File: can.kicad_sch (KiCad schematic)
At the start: 4 parts, among them U8 SN65HVD230

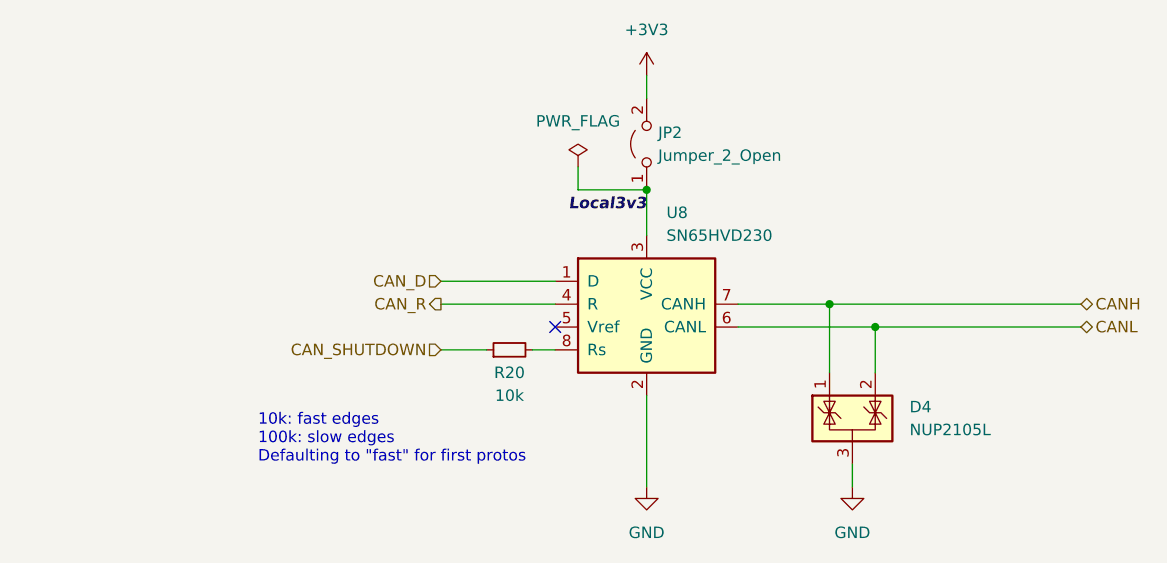
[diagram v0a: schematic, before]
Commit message: push forwards: clock muxing, filling in blanks
Finished off the ethernet section finally.
Sorted a solution to the 25M phy clocks required for ethercat
Connected CAN as per existing hardware (and fixed a bug in speed mode)
Sorted out bypassing for MCU
Added more thoughts on the external interfaces
Started on a 24V supply
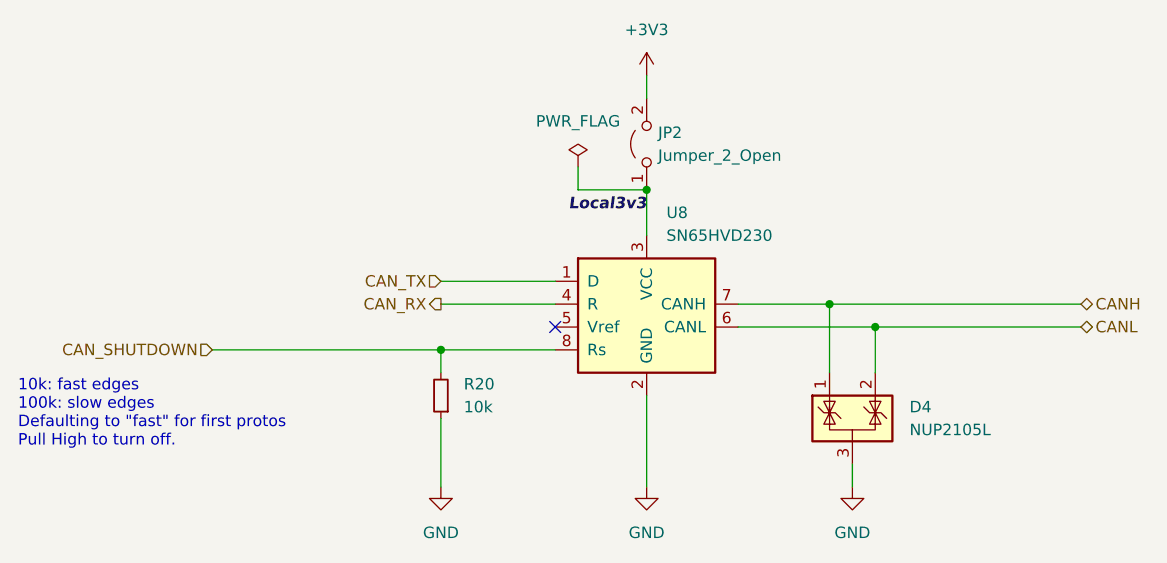
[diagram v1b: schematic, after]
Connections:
- net CAN_SHUTDOWN: now also R20.2, U8.8 (Rs); no longer R20.1
- net GND: now also R20.1
- net CAN_D renamed CAN_TX
- net CAN_R renamed CAN_RX
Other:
- note added: "10k: fast edges 100k: slow edges Defaulting to "fast" for first protos Pull High to turn off."
- note removed: "10k: fast edges 100k: slow edges Defaulting to "fast" for first protos"
- moved on the sheet: R20
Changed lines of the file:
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@@
 	(generator_version "10.0")
 	(paper "A4")
-	(text "10k: fast edges\n100k: slow edges\nDefaulting to \"fast\" for first protos"
+	(text "10k: fast edges\n100k: slow edges\nDefaulting to \"fast\" for first protos\nPull High to turn off."
 		(exclude_from_sim no)
-		(at 81.28 106.68 0)
+		(at 54.61 104.902 0)
 		(effects
 			(font
@@
 			(justify left bottom)
 		)
+	)
+	(junction
+		(at 101.6 93.98)
+		(diameter 0)
+		(color 0 0 0 0)
 	)
 	(junction
@@
 	(wire
 		(pts
-			(xy 101.6 93.98) (xy 106.68 93.98)
-		)
-		(stroke
-			(width 0)
-			(type default)
-		)
-	)
-	(wire
-		(pts
-			(xy 111.76 93.98) (xy 114.3 93.98)
+			(xy 76.2 93.98) (xy 101.6 93.98)
 		)
 		(stroke
@@
 	(wire
 		(pts
+			(xy 101.6 93.98) (xy 114.3 93.98)
+		)
+		(stroke
+			(width 0)
+			(type default)
+		)
+	)
+	(wire
+		(pts
 			(xy 149.86 91.44) (xy 149.86 96.52)
 		)
@@
 	(wire
 		(pts
+			(xy 101.6 101.6) (xy 101.6 109.22)
+		)
+		(stroke
+			(width 0)
+			(type default)
+		)
+	)
+	(wire
+		(pts
 			(xy 144.78 88.9) (xy 172.72 88.9)
 		)
@@
 		(pts
 			(xy 116.84 76.2) (xy 124.46 76.2)
+		)
+		(stroke
+			(width 0)
+			(type default)
+		)
+	)
+	(wire
+		(pts
+			(xy 101.6 96.52) (xy 101.6 93.98)
 		)
 		(stroke
@@
 	(hierarchical_label "CAN_SHUTDOWN"
 		(shape input)
-		(at 101.6 93.98 180)
+		(at 76.2 93.98 180)
 		(effects
 			(font
@@
 		)
 	)
-	(hierarchical_label "CAN_D"
+	(hierarchical_label "CAN_TX"
 		(shape input)
 		(at 101.6 86.36 180)
@@
 		)
 	)
-	(hierarchical_label "CAN_R"
+	(hierarchical_label "CAN_RX"
 		(shape output)
 		(at 101.6 88.9 180)
@@
 	(symbol
 		(lib_id "Device:R_Small")
-		(at 109.22 93.98 90)
+		(at 101.6 99.06 180)
 		(unit 1)
 		(body_style 1)
@@
 		(fields_autoplaced yes)
 		(property "Reference" "R20"
-			(at 109.22 96.52 90)
-			(show_name no)
-			(do_not_autoplace no)
-			(effects
-				(font
-					(size 1.27 1.27)
-				)
+			(at 104.14 97.7899 0)
+			(show_name no)
+			(do_not_autoplace no)
+			(effects
+				(font
+					(size 1.27 1.27)
+				)
+				(justify right)
 			)
 		)
 		(property "Value" "10k"
-			(at 109.22 99.06 90)
-			(show_name no)
-			(do_not_autoplace no)
-			(effects
-				(font
-					(size 1.27 1.27)
-				)
+			(at 104.14 100.3299 0)
+			(show_name no)
+			(do_not_autoplace no)
+			(effects
+				(font
+					(size 1.27 1.27)
+				)
+				(justify right)
 			)
 		)
 		(property "Footprint" "Resistor_SMD:R_0603_1608Metric"
-			(at 109.22 93.98 0)
+			(at 101.6 99.06 0)
 			(hide yes)
 			(show_name no)
@@
 		)
 		(property "Datasheet" ""
-			(at 109.22 93.98 0)
+			(at 101.6 99.06 0)
 			(hide yes)
 			(show_name no)
@@
 		)
 		(property "Description" ""
-			(at 109.22 93.98 0)
+			(at 101.6 99.06 0)
 			(show_name no)
 			(do_not_autoplace no)
@@
 		)
 		(property "MPN" "0603WAF1002T5E"
-			(at 109.22 93.98 0)
+			(at 101.6 99.06 0)
 			(hide yes)
 			(show_name no)
@@
 		)
 		(property "jlc-basic" "1"
-			(at 109.22 93.98 0)
+			(at 101.6 99.06 0)
 			(hide yes)
 			(show_name no)
@@
 		)
 		(property "lcsc#" "C25804"
-			(at 109.22 93.98 0)
+			(at 101.6 99.06 0)
 			(hide yes)
 			(show_name no)
@@
 		)
 		(property "lcsc2#" ""
-			(at 109.22 93.98 0)
+			(at 101.6 99.06 0)
 			(hide yes)
 			(show_name no)
@@
 					(unit 1)
 				)
+			)
+		)
+	)
+	(symbol
+		(lib_id "power:GND")
+		(at 101.6 109.22 0)
+		(unit 1)
+		(body_style 1)
+		(exclude_from_sim no)
+		(in_bom yes)
+		(on_board yes)
+		(in_pos_files yes)
+		(dnp no)
+		(fields_autoplaced yes)
+		(property "Reference" "#PWR062"
+			(at 101.6 115.57 0)
+			(hide yes)
+			(show_name no)
+			(do_not_autoplace no)
+			(effects
+				(font
+					(size 1.27 1.27)
+				)
+			)
+		)
+		(property "Value" "GND"
+			(at 101.6 114.3 0)
+			(show_name no)
+			(do_not_autoplace no)
+			(effects
+				(font
+					(size 1.27 1.27)
+				)
+			)
+		)
+		(property "Footprint" ""
+			(at 101.6 109.22 0)
+			(hide yes)
+			(show_name no)
+			(do_not_autoplace no)
+			(effects
+				(font
+					(size 1.27 1.27)
+				)
+			)
+		)
+		(property "Datasheet" ""
+			(at 101.6 109.22 0)
+			(hide yes)
+			(show_name no)
+			(do_not_autoplace no)
+			(effects
+				(font
+					(size 1.27 1.27)
+				)
+			)
+		)
+		(property "Description" ""
+			(at 101.6 109.22 0)
+			(show_name no)
+			(do_not_autoplace no)
+			(effects
+				(font
+					(size 1.27 1.27)
+				)
+			)
+		)
+		(pin "1"
+		)
+		(instances
+			(project "xmc-ecat-enet-twin"
+				(path "/f5c7c34d-e330-4aa5-be7e-80f0a3a977af/ad8b4270-a50e-4348-8863-ac523723f700"
+					(reference "#PWR062")
+					(unit 1)
+				)

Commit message: finish a 24V supply
went with a more modern one, plenty of room.  Should be pretty good now.
Went over and filled in a bunch of missing parts and things, cleaned up
as much as I could 0603 vs 0402 for most, updated some thigns to current
atomic part library.

still to go, the "pi" interface and some sort of spi/io interface?
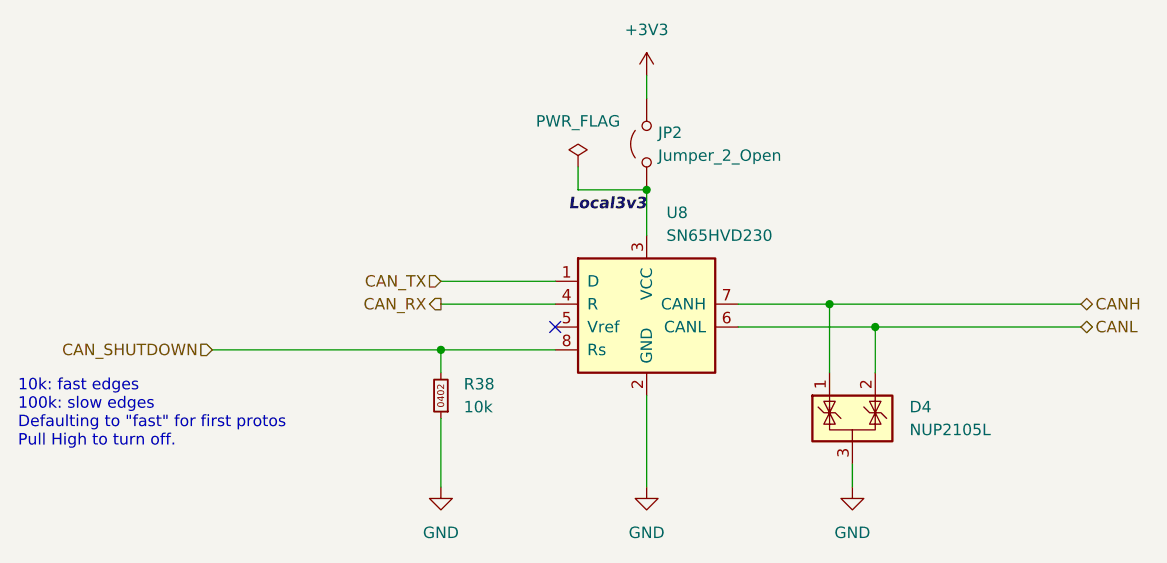
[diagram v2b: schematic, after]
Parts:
- removed R20: 10k, Resistor_SMD:R_0603_1608Metric, symbol Device:R_Small
- added R38: 10k, Resistor_SMD:R_0402_1005Metric, symbol karl-atomic-basic:KR0402_10k
- D4: LCSC Part # (none) -> C5261087; jlc-basic 0 -> (none); jlcbasic (none) -> 0; lcsc# C5261087 -> (none)
- U8: LCSC Part # (none) -> C12084; jlc-basic 1 -> (none); jlcbasic (none) -> basic; lcsc# C12084 -> (none)
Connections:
- net CAN_SHUTDOWN: now also R38.2
- net GND: now also R38.1
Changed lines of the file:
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@@
 	(wire
 		(pts
-			(xy 101.6 96.52) (xy 101.6 93.98)
+			(xy 149.86 91.44) (xy 172.72 91.44)
 		)
 		(stroke
@@
 	(wire
 		(pts
-			(xy 149.86 91.44) (xy 172.72 91.44)
+			(xy 101.6 93.98) (xy 101.6 96.52)
 		)
 		(stroke
@@
 	)
 	(symbol
-		(lib_id "Device:R_Small")
+		(lib_id "karl-atomic-basic:KR0402_10k")
 		(at 101.6 99.06 180)
 		(unit 1)
@@
 		(dnp no)
 		(fields_autoplaced yes)
-		(property "Reference" "R20"
+		(property "Reference" "R38"
 			(at 104.14 97.7899 0)
 			(show_name no)
@@
 			)
 		)
-		(property "Footprint" "Resistor_SMD:R_0603_1608Metric"
+		(property "Footprint" "Resistor_SMD:R_0402_1005Metric"
 			(at 101.6 99.06 0)
 			(hide yes)
@@
 			)
 		)
-		(property "Description" ""
+		(property "Description" "Resistor, 0402"
 			(at 101.6 99.06 0)
-			(show_name no)
-			(do_not_autoplace no)
-			(effects
-				(font
-					(size 1.27 1.27)
-				)
-			)
-		)
-		(property "MPN" "0603WAF1002T5E"
+			(hide yes)
+			(show_name no)
+			(do_not_autoplace no)
+			(effects
+				(font
+					(size 1.27 1.27)
+				)
+			)
+		)
+		(property "LCSC Part #" "C25744"
 			(at 101.6 99.06 0)
 			(hide yes)
@@
 			)
 		)
-		(property "jlc-basic" "1"
+		(property "MPN" "0402WGF1002TCE"
 			(at 101.6 99.06 0)
 			(hide yes)
@@
 			)
 		)
-		(property "lcsc#" "C25804"
+		(property "jlcbasic" "basic"
 			(at 101.6 99.06 0)
 			(hide yes)
@@
 			)
 		)
-		(property "lcsc2#" ""
+		(property "JLCbasic" ""
+			(at 101.6 99.06 90)
+			(hide yes)
+			(show_name no)
+			(do_not_autoplace no)
+			(effects
+				(font
+					(size 1.27 1.27)
+				)
+			)
+		)
+		(property "jlc-basic" ""
+			(at 101.6 99.06 0)
+			(hide yes)
+			(show_name no)
+			(do_not_autoplace no)
+			(effects
+				(font
+					(size 1.27 1.27)
+				)
+			)
+		)
+		(property "lcsc#" ""
 			(at 101.6 99.06 0)
 			(hide yes)
@@
 			(project "xmc-ecat-enet-twin"
 				(path "/f5c7c34d-e330-4aa5-be7e-80f0a3a977af/ad8b4270-a50e-4348-8863-ac523723f700"
-					(reference "R20")
+					(reference "R38")
 					(unit 1)
 				)
@@
 			)
 		)
-		(property "Description" ""
+		(property "Description" "CAN Bus Transceivers, 3.3V, 1Mbps, Low-Power capabilities, SOIC-8"
 			(at 124.46 88.9 0)
-			(show_name no)
-			(do_not_autoplace no)
-			(effects
-				(font
-					(size 1.27 1.27)
-				)
-			)
-		)
-		(property "lcsc#" "C12084"
+			(hide yes)
+			(show_name no)
+			(do_not_autoplace no)
+			(effects
+				(font
+					(size 1.27 1.27)
+				)
+			)
+		)
+		(property "LCSC Part #" "C12084"
 			(at 124.46 88.9 0)
 			(hide yes)
@@
 			)
 		)
-		(property "jlc-basic" "1"
+		(property "lcsc2#" ""
 			(at 124.46 88.9 0)
 			(hide yes)
@@
 			)
 		)
-		(property "lcsc2#" ""
+		(property "jlcbasic" "basic"
+			(at 124.46 88.9 0)
+			(hide yes)
+			(show_name no)
+			(do_not_autoplace no)
+			(effects
+				(font
+					(size 1.27 1.27)
+				)
+			)
+		)
+		(property "lcsc#" ""
 			(at 124.46 88.9 0)
 			(hide yes)
@@
 			)
 		)
-		(property "Description" ""
+		(property "Description" "Power symbol creates a global label with name \"GND\" , ground"
 			(at 147.32 109.22 0)
+			(hide yes)
 			(show_name no)
 			(do_not_autoplace no)
@@
 			)
 		)
-		(property "Description" ""
+		(property "Description" "Power symbol creates a global label with name \"+3V3\""
 			(at 124.46 63.5 0)
+			(hide yes)
 			(show_name no)
 			(do_not_autoplace no)
@@
 			)
 		)
-		(property "Description" ""
+		(property "Description" "Special symbol for telling ERC where power comes from"
 			(at 116.84 73.66 0)
+			(hide yes)
 			(show_name no)
 			(do_not_autoplace no)
@@
 			)
 		)
-		(property "Description" ""
+		(property "Description" "Power symbol creates a global label with name \"GND\" , ground"
 			(at 101.6 109.22 0)
+			(hide yes)
 			(show_name no)
 			(do_not_autoplace no)
@@
 			)
 		)
-		(property "Description" ""
+		(property "Description" "Jumper, 2-pole, open"
 			(at 124.46 71.12 0)
+			(hide yes)
+			(show_name no)
+			(do_not_autoplace no)
+			(effects
+				(font
+					(size 1.27 1.27)
+				)
+			)
+		)
+		(property "JLCbasic" ""
+			(at 124.46 71.12 90)
+			(hide yes)
+			(show_name no)
+			(do_not_autoplace no)
+			(effects
+				(font
+					(size 1.27 1.27)
+				)
+			)
+		)
+		(property "jlc-basic" ""
+			(at 124.46 71.12 90)
+			(hide yes)
+			(show_name no)
+			(do_not_autoplace no)
+			(effects
+				(font
+					(size 1.27 1.27)
+				)
+			)
+		)
+		(property "lcsc#" ""
+			(at 124.46 71.12 90)
+			(hide yes)
 			(show_name no)
 			(do_not_autoplace no)
@@
 			)
 		)
-		(property "Datasheet" "http://www.onsemi.com/pub_link/Collateral/NUP2105L-D.PDF"
+		(property "Datasheet" "https://www.onsemi.com/pub_link/Collateral/NUP2105L-D.PDF"
 			(at 150.495 98.425 0)
 			(hide yes)
@@
 			)
 		)
-		(property "Description" ""
+		(property "Description" "Dual Line CAN Bus Protector, 24Vrwm"
 			(at 147.32 101.6 0)
+			(hide yes)
 			(show_name no)
 			(do_not_autoplace no)
@@
 			)
 		)
-		(property "jlc-basic" "0"
+		(property "LCSC Part #" "C5261087"
 			(at 147.32 101.6 0)
 			(hide yes)
@@
 			)
 		)
-		(property "lcsc#" "C5261087"
+		(property "jlcbasic" "0"
 			(at 147.32 101.6 0)
 			(hide yes)
@@
 			)
 		)
-		(property "lcsc2#" ""
+		(property "lcsc#" ""
 			(at 147.32 101.6 0)
 			(hide yes)
@@
 			)
 		)
-		(property "Description" ""
+		(property "Description" "Power symbol creates a global label with name \"GND\" , ground"
 			(at 124.46 109.22 0)
-			(show_name no)
-			(do_not_autoplace no)
+			(hide yes)
+			(show_name no)
+			(do_not_autoplace no)
